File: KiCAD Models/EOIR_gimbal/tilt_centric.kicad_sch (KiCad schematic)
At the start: 3 parts, among them J5 RJ45, U14 RPI4B

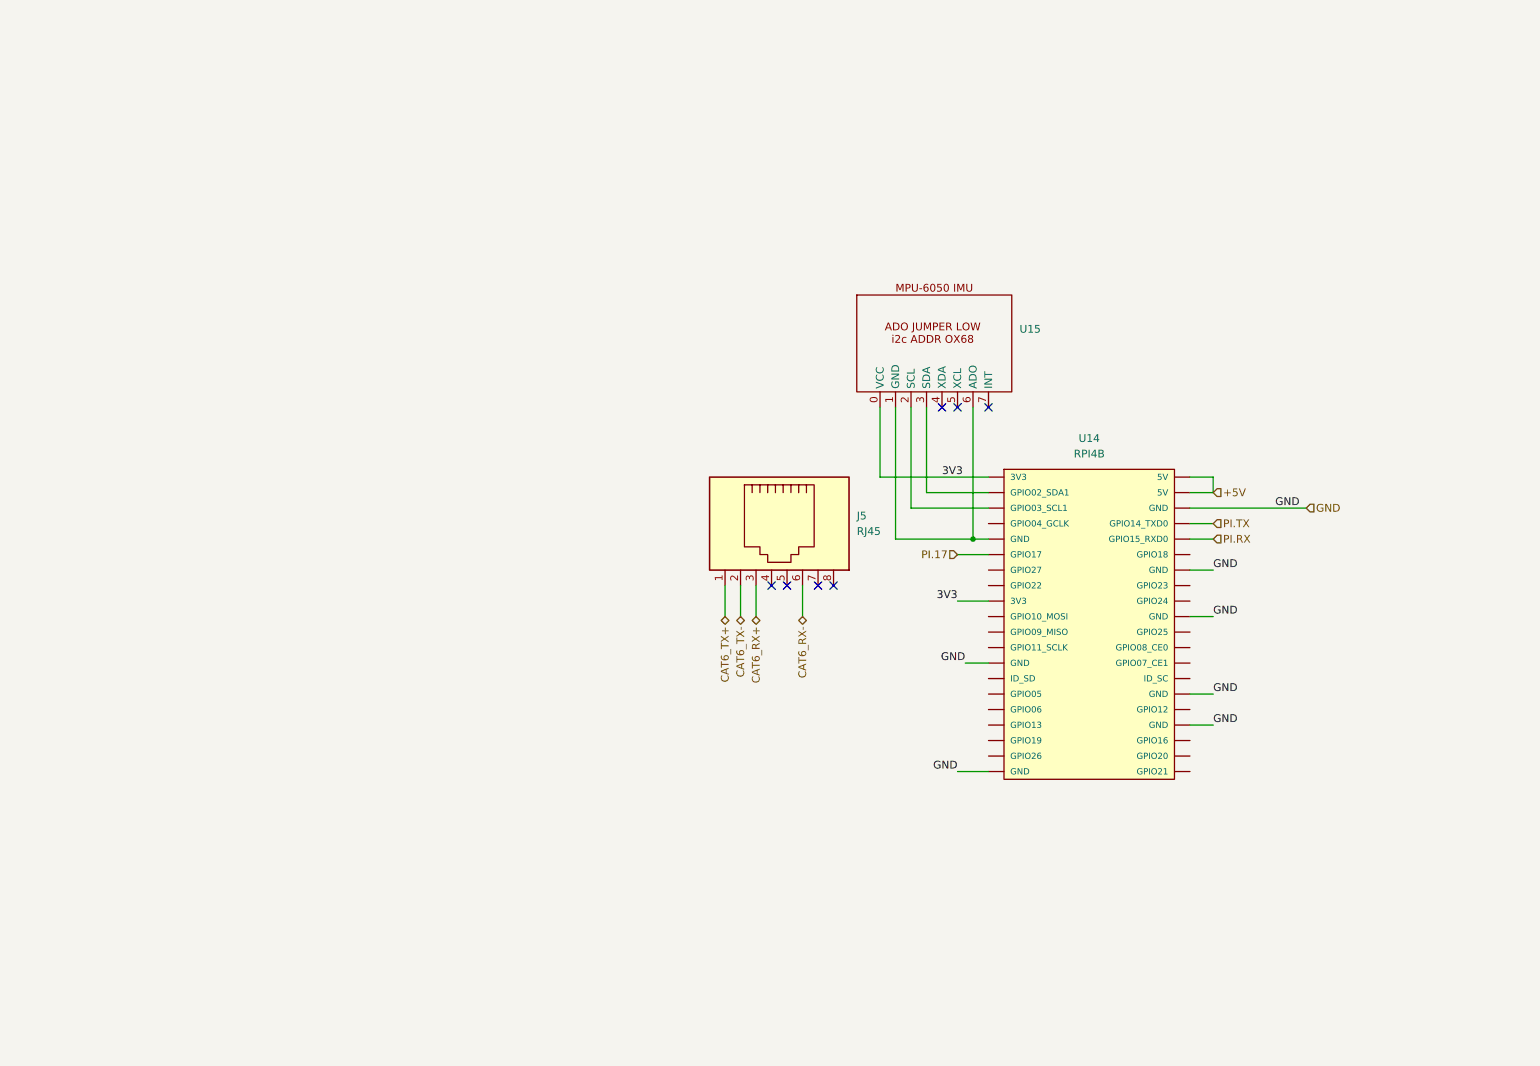
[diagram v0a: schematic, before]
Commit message: KiCAD: update schematics — TMC2209 pinout, GPS, lens controller wiring
Co-Authored-By: Claude Sonnet 4.6 <noreply@anthropic.com>
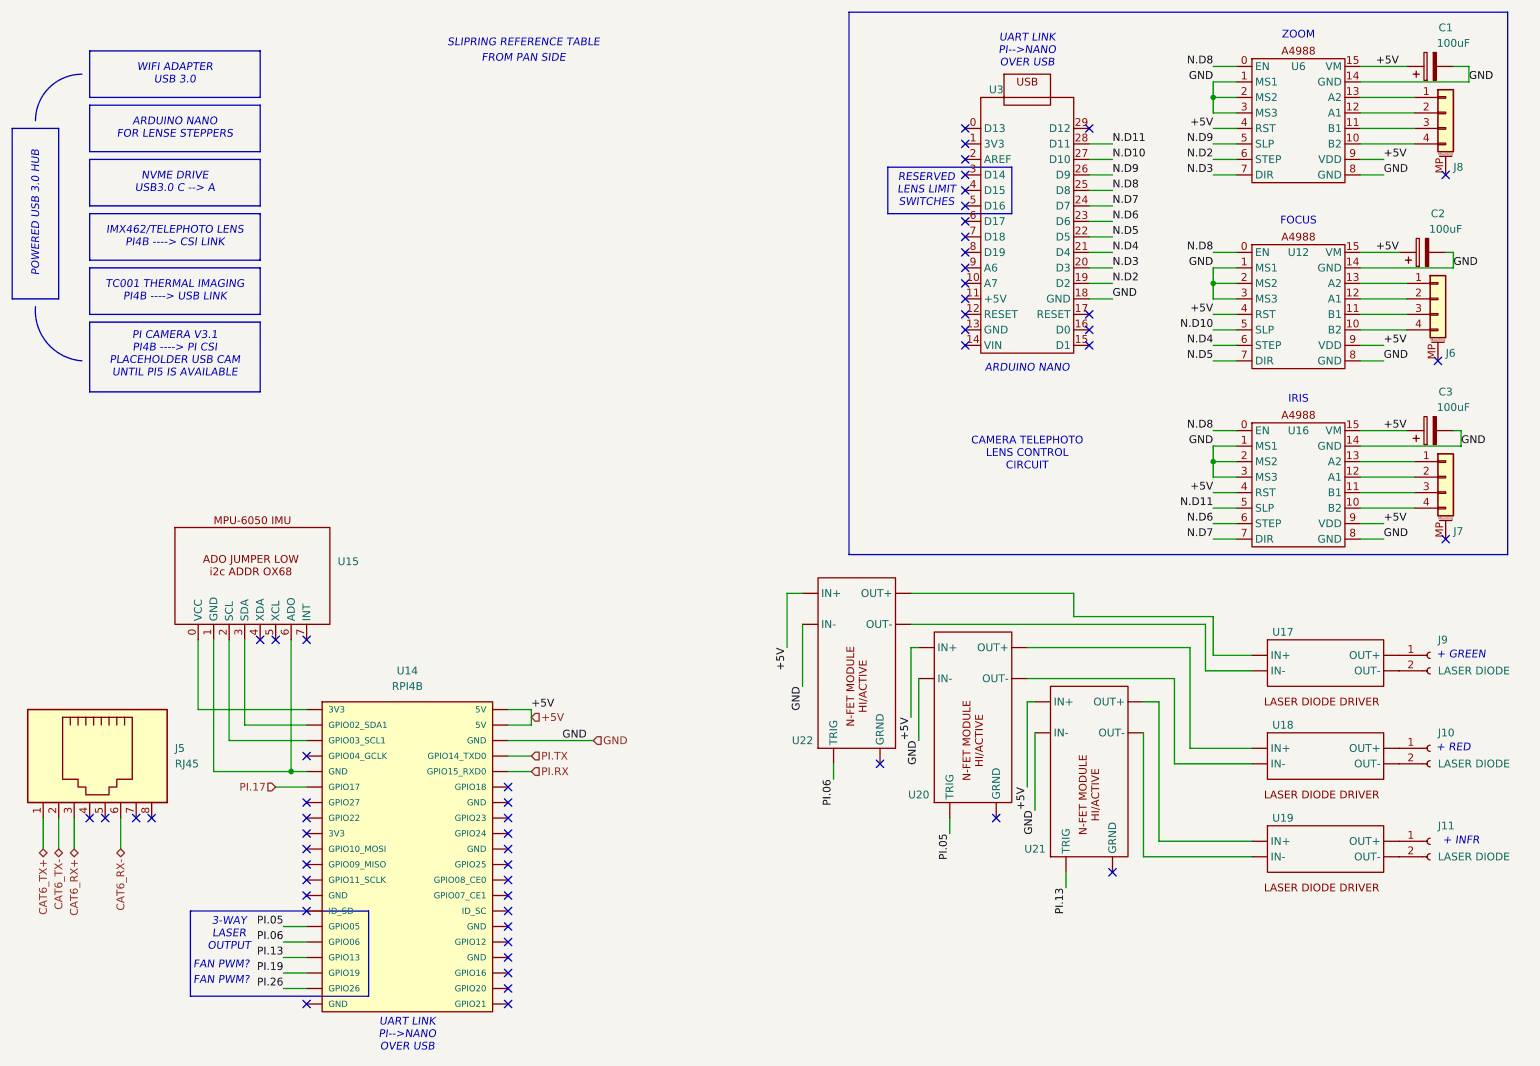
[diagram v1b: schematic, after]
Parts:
- added C1, C2, C3: 100uF, symbol Device:C_Polarized
- added J10, J11, J9: LASER DIODE, symbol Connector:Conn_01x02_Socket
- added J6, J7, J8: ~, symbol Connector_Generic_MountingPin:Conn_01x04_MountingPin
- added U12, U16, U6: ~, symbol gimbal_project:A4988_DRIVER
- added U17, U18, U19: ~, symbol gimbal_project:LASER_DRIVER
- added U20, U21, U22: ~, symbol gimbal_project:MOSFET_MOD
- added U3: ~, symbol gimbal_project:Arduino_Nano
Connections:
- net +5V: now also C1.1, C2.1, C3.1, U12.15 (VM), U12.4 (RST), U12.9 (VDD), U16.15 (VM), U16.4 (RST), U16.9 (VDD), U20. (OUT+), U21. (OUT+), U22. (OUT+), U6.15 (VM), U6.4 (RST), U6.9 (VDD)
- net GND: now also C1.2, C2.2, C3.2, U12.1 (MS1), U12.14 (GND), U12.2 (MS2), U12.3 (MS3), U12.8 (GND), U16.1 (MS1), U16.14 (GND), U16.2 (MS2), U16.3 (MS3), U16.8 (GND), U20. (OUT+), U21. (OUT+), U22. (OUT+), U3.18 (GND), U6.1 (MS1), U6.14 (GND), U6.2 (MS2), U6.3 (MS3), U6.8 (GND); no longer U14.14 (GND), U14.20 (GND), U14.25 (GND), U14.30 (GND), U14.34 (GND), U14.39 (GND)
- net PI.05: now reaches U14.29 (GPIO05)
- net PI.05: now also U20. (OUT+)
- net PI.06: now reaches U14.31 (GPIO06)
- net PI.06: now also U22. (OUT+)
- net PI.13: now reaches U14.33 (GPIO13)
- net PI.13: now also U21. (OUT+)
- net PI.19: now reaches U14.35 (GPIO19)
- net PI.26: now reaches U14.37 (GPIO26)
- net 3V3: no longer names the net of U14.1 (3V3), U15.0 (VCC)
- net 3V3: no longer U14.17 (3V3)
- new net: J6.1 (Pin_1), U12.13 (A2)
- new net: J6.2 (Pin_2), U12.12 (A1)
- new net: J6.3 (Pin_3), U12.11 (B1)
- new net: J6.4 (Pin_4), U12.10 (B2)
- new net: U19. (OUT-), U21. (OUT+) (x2)
- new net: J8.1 (Pin_1), U6.13 (A2)
- new net: J8.2 (Pin_2), U6.12 (A1)
- new net: J8.3 (Pin_3), U6.11 (B1)
- new net: J8.4 (Pin_4), U6.10 (B2)
- new net: J11.1 (Pin_1), U19. (OUT-)
- new net: J11.2 (Pin_2), U19. (OUT-)
- new net: U18. (OUT-), U20. (OUT+) (x2)
- new net: U17. (OUT-), U22. (OUT+) (x2)
- new net: J9.1 (Pin_1), U17. (OUT-)
- new net: J9.2 (Pin_2), U17. (OUT-)
- new net: J7.1 (Pin_1), U16.13 (A2)
- new net: J7.2 (Pin_2), U16.12 (A1)
- new net: J7.3 (Pin_3), U16.11 (B1)
- new net: J7.4 (Pin_4), U16.10 (B2)
- new net: J10.1 (Pin_1), U18. (OUT-)
- new net: J10.2 (Pin_2), U18. (OUT-)
- new net N.D10: U12.5 (SLP), U3.27 (D10)
- new net N.D11: U16.5 (SLP), U3.28 (D11)
- new net N.D2: U3.19 (D2), U6.6 (STEP)
- new net N.D3: U3.20 (D3), U6.7 (DIR)
- new net N.D4: U12.6 (STEP), U3.21 (D4)
- new net N.D5: U12.7 (DIR), U3.22 (D5)
- new net N.D6: U16.6 (STEP), U3.23 (D6)
- new net N.D7: U16.7 (DIR), U3.24 (D7)
- new net N.D8: U12.0 (EN), U16.0 (EN), U3.25 (D8), U6.0 (EN)
- new net N.D9: U3.26 (D9), U6.5 (SLP)
- no-connect marks 7 -> 57
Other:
- note added: "+ GREEN"
- note added: "+ INFR"
- note added: "+ RED"
- note added: "3-WAY LASER OUTPUT"
- note added: "ARDUINO NANO"
- note added: "ARDUINO NANO FOR LENSE STEPPERS"
- note added: "CAMERA TELEPHOTO LENS CONTROL CIRCUIT"
- note added: "FAN PWM?"
- note added: "FOCUS"
- note added: "FROM PAN SIDE"
- note added: "IMX462/TELEPHOTO LENS PI4B ----> CSI LINK"
- note added: "IRIS"
- note added: "NVME DRIVE USB3.0 C --> A"
- note added: "PI CAMERA V3.1 PI4B ----> PI CSI PLACEHOLDER USB CAM UNTIL PI5 IS AVAILABLE"
- note added: "POWERED USB 3.0 HUB"
- note added: "RESERVED LENS LIMIT SWITCHES"
- note added: "SLIPRING REFERENCE TABLE"
- note added: "TC001 THERMAL IMAGING PI4B ----> USB LINK"
- note added: "UART LINK PI-->NANO OVER USB"
- note added: "WIFI ADAPTER USB 3.0"
- note added: "ZOOM"
- moved on the sheet: J5, U14, U15
